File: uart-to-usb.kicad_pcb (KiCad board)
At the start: 2 copper layers, 43.5 x 29.5 mm, 9 parts, among them J1 USB_C_Receptacle_USB2.0_16P, U1 FT232RL

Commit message: Initial PCB route
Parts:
- added J2: Conn_01x02_Pin, Connector_JST:JST_GH_SM02B-GHS-TB_1x02-1MP_P1.25mm_Horizontal, F.Cu at (159.8, 94.0)
- added J3: Conn_01x02_Pin, Connector_PinSocket_2.00mm:PinSocket_1x02_P2.00mm_Horizontal, F.Cu at (155.2, 101.0)
- moved C3 9.24 mm to (142.0, 98.5)
- moved C4 8.95 mm to (135.0, 100.5), turned to -90 degrees
- moved C2 8.54 mm to (139.5, 99.0)
- moved C1 7.43 mm to (140.0, 95.5), turned to 180 degrees
- moved U1 5.22 mm to (148.0, 96.5)
- moved R1 4.53 mm to (134.5, 97.5), turned to 0 degrees
- moved FB1 2.50 mm to (137.5, 98.5), turned to -90 degrees
- moved R2 1.00 mm to (135.0, 93.0), turned to 90 degrees
- moved J1 0.50 mm to (127.5, 96.5)
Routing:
- net unconnected-(J1-SHIELD-PadSH): track 0.00 -> 17.0 mm
- net +5V: track 0.00 -> 14.6 mm
- net Net-(J2-Pin_1): track 0.00 -> 12.9 mm, vias 0 -> 1
- net Net-(J2-Pin_2): track 0.00 -> 11.7 mm
- net /D+: track 9.85 -> 17.4 mm, vias 0 -> 2
- net /D-: track 9.78 -> 16.9 mm, vias 0 -> 2
- net Net-(U1-3V3OUT): track 0.00 -> 4.33 mm
- net Net-(J1-CC2): track 0.00 -> 2.72 mm
- net Net-(C4-Pad1): track 4.45 -> 6.07 mm
- added copper zone on B.Cu, net GND
- added copper zone on F.Cu, net GND
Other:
- board size 43.5 x 29.5 mm -> 39.5 x 14 mm

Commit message: Add profile
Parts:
- added G***: LOGO, LOGO, F.Cu at (137.5, 90.7)
- moved J2 0.43 mm to (160.3, 94.0)
- moved J3 0.21 mm to (155.4, 101.1)
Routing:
- net Net-(J2-Pin_2): track 11.7 -> 12.3 mm
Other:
- board text added: "@kj-49"

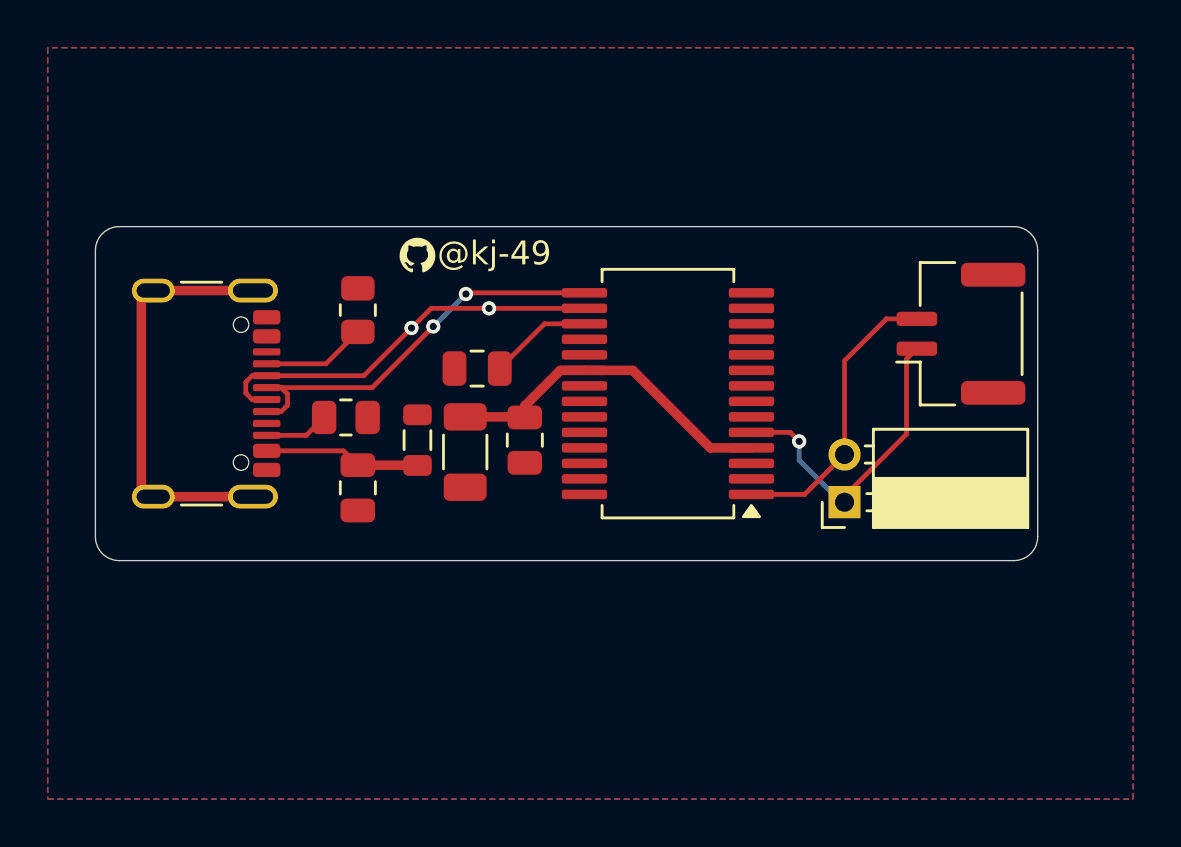
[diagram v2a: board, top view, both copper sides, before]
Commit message: Use single input connector
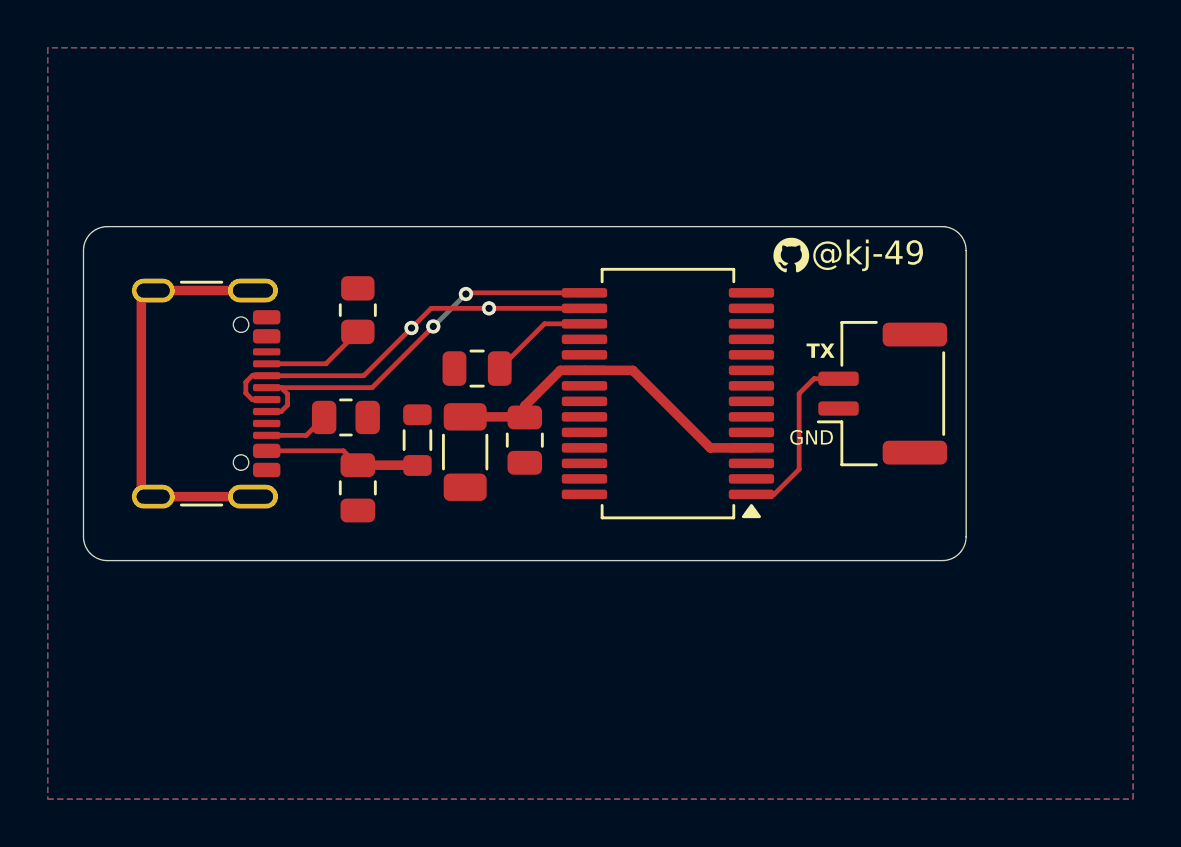
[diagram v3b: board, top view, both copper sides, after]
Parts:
- removed J3: Conn_01x02_Pin, Connector_PinSocket_2.00mm:PinSocket_1x02_P2.00mm_Horizontal
- moved G*** 15.7 mm to (153.2, 90.7)
- moved J2 4.13 mm to (157.0, 96.5)
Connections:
- J2 pad 1: Net-(J2-Pin_1) -> GND
- U1 pad 5: Net-(J2-Pin_1) -> unconnected-(U1-RXD-Pad5)
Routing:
- net Net-(J2-Pin_1): track 13.1 -> 0.00 mm, vias 1 -> 0
- net Net-(J2-Pin_2): track 12.3 -> 7.52 mm
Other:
- board size 39.5 x 14 mm -> 37 x 14 mm
- board text added: "GND"
- board text added: "TX"
